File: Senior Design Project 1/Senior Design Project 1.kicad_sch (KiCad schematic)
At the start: 18 parts, among them SW1 SW_Nidec_CAS-120A1, U1 74LS05, U10 74LS08, U11 74LS08, U12 74LS08, U13 74LS08, U2 74HC273, U3 74HC74, U4 74HC74, U5 74HC74, U6 74HC74, U7 74HC74, U8 74HC74, U9 74HC273

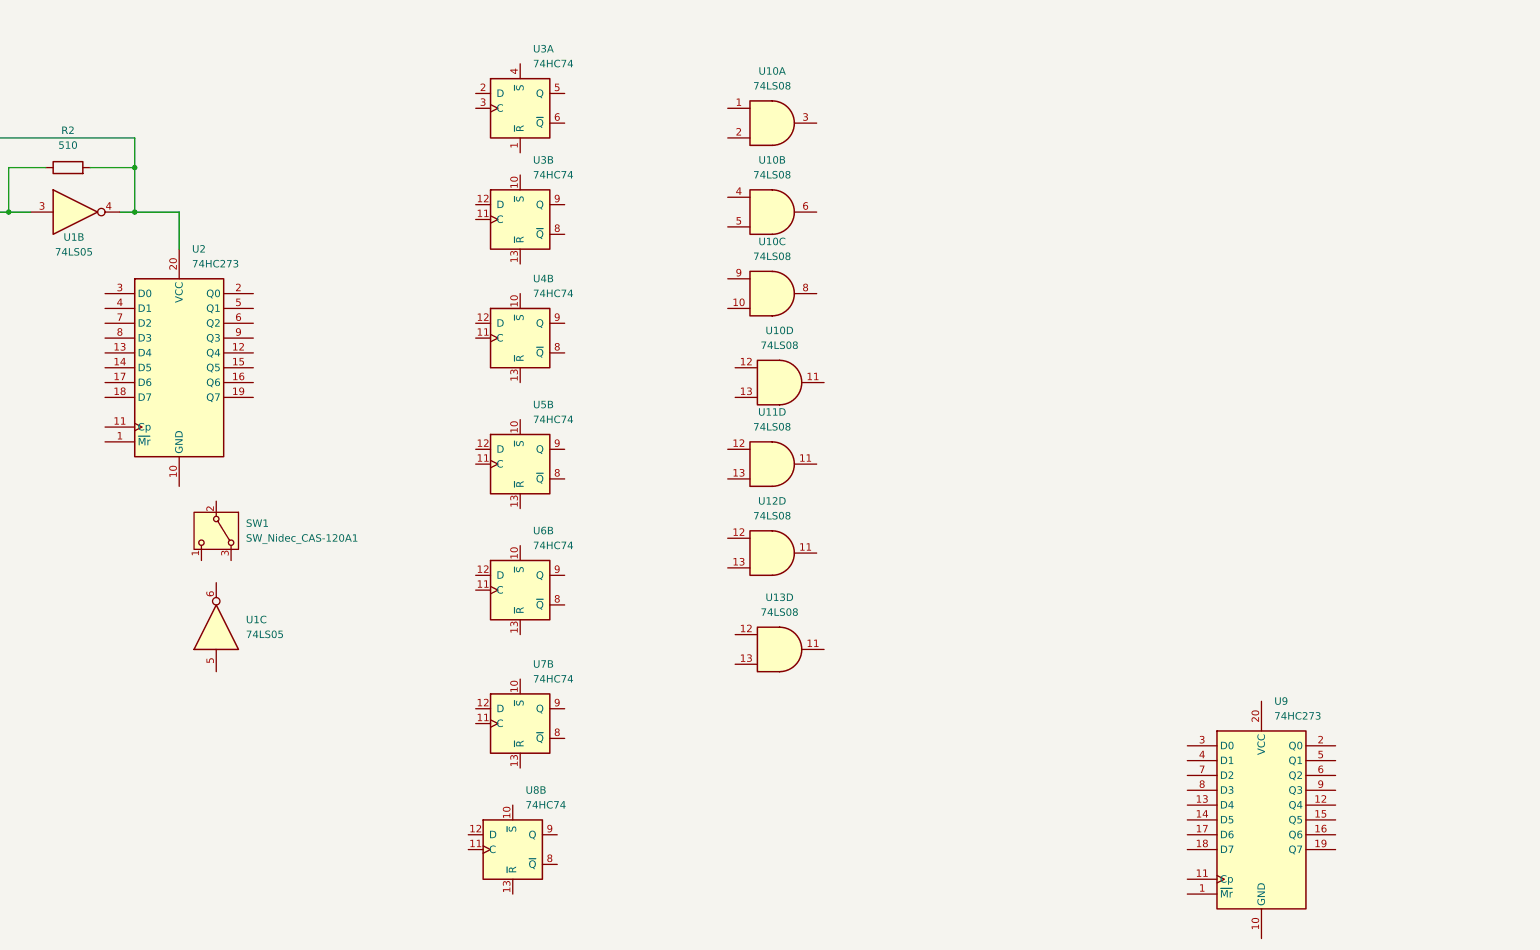
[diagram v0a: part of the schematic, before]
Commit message: Added components & footprints
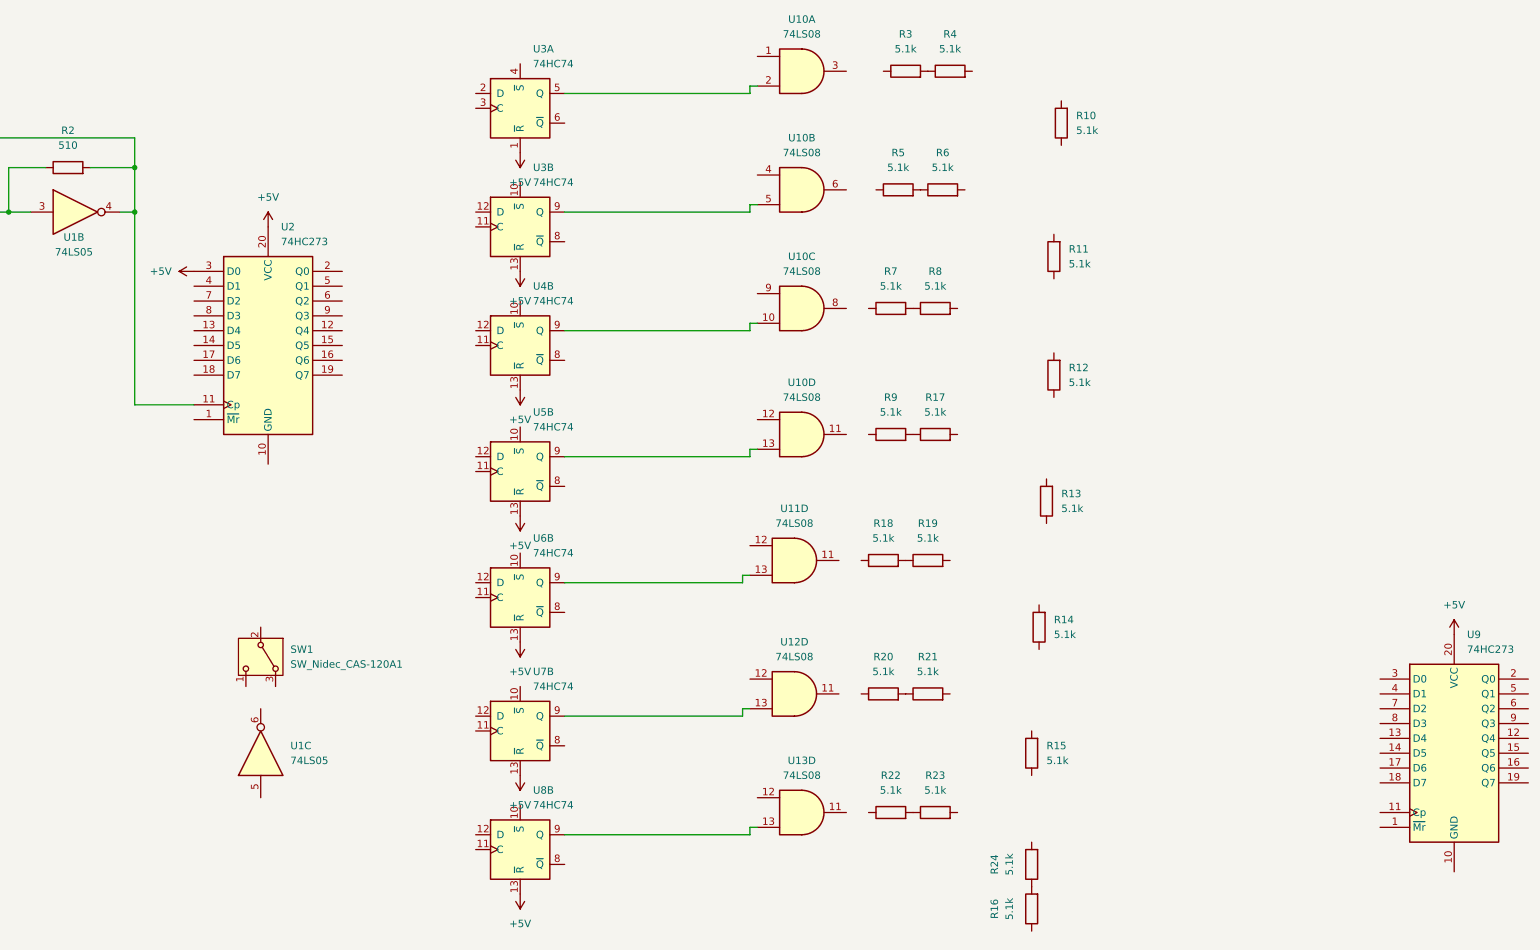
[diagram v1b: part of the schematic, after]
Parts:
- added R10, R11, R12, R13, R14, R15, R16, R17, R18, R19, R20, R21, R22, R23, R24, R3, R4, R5, R6, R7, R8, R9: 5.1k, Resistor_THT:R_Axial_DIN0204_L3.6mm_D1.6mm_P7.62mm_Horizontal, symbol Device:R
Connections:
- net +5V: now reaches U3.13 (~{R})
- net +5V: now also U2.20 (VCC), U2.3 (D0), U3.1 (~{R}), U4.13 (~{R}), U5.13 (~{R}), U6.13 (~{R}), U7.13 (~{R}), U8.13 (~{R}), U9.20 (VCC)
- net at U3.9 (Q): now also U10.5
- net at U10.2: now also U3.5 (Q)
- net at U11.13: now also U6.9 (Q)
- net at C2.2, R2.2, U1.4: now also U2.11 (Cp); no longer U2.20 (VCC)
- net at U13.13: now also U8.9 (Q)
- net at U7.9 (Q): now also U12.13
- net at U4.9 (Q): now also U10.10
- net at U10.13: now also U5.9 (Q)
- new net: R20.2, R21.1
- new net: R22.2, R23.1
- new net: R7.2, R8.1
- new net: R5.2, R6.1
- new net: R16.2, R24.1
- new net: R18.2, R19.1
- new net: R17.1, R9.2
- new net: R3.2, R4.1
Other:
- moved on the sheet: SW1, U10A, U10B, U10C, U10D, U11D, U12D, U13D, U1C, U2, U3B, U4B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

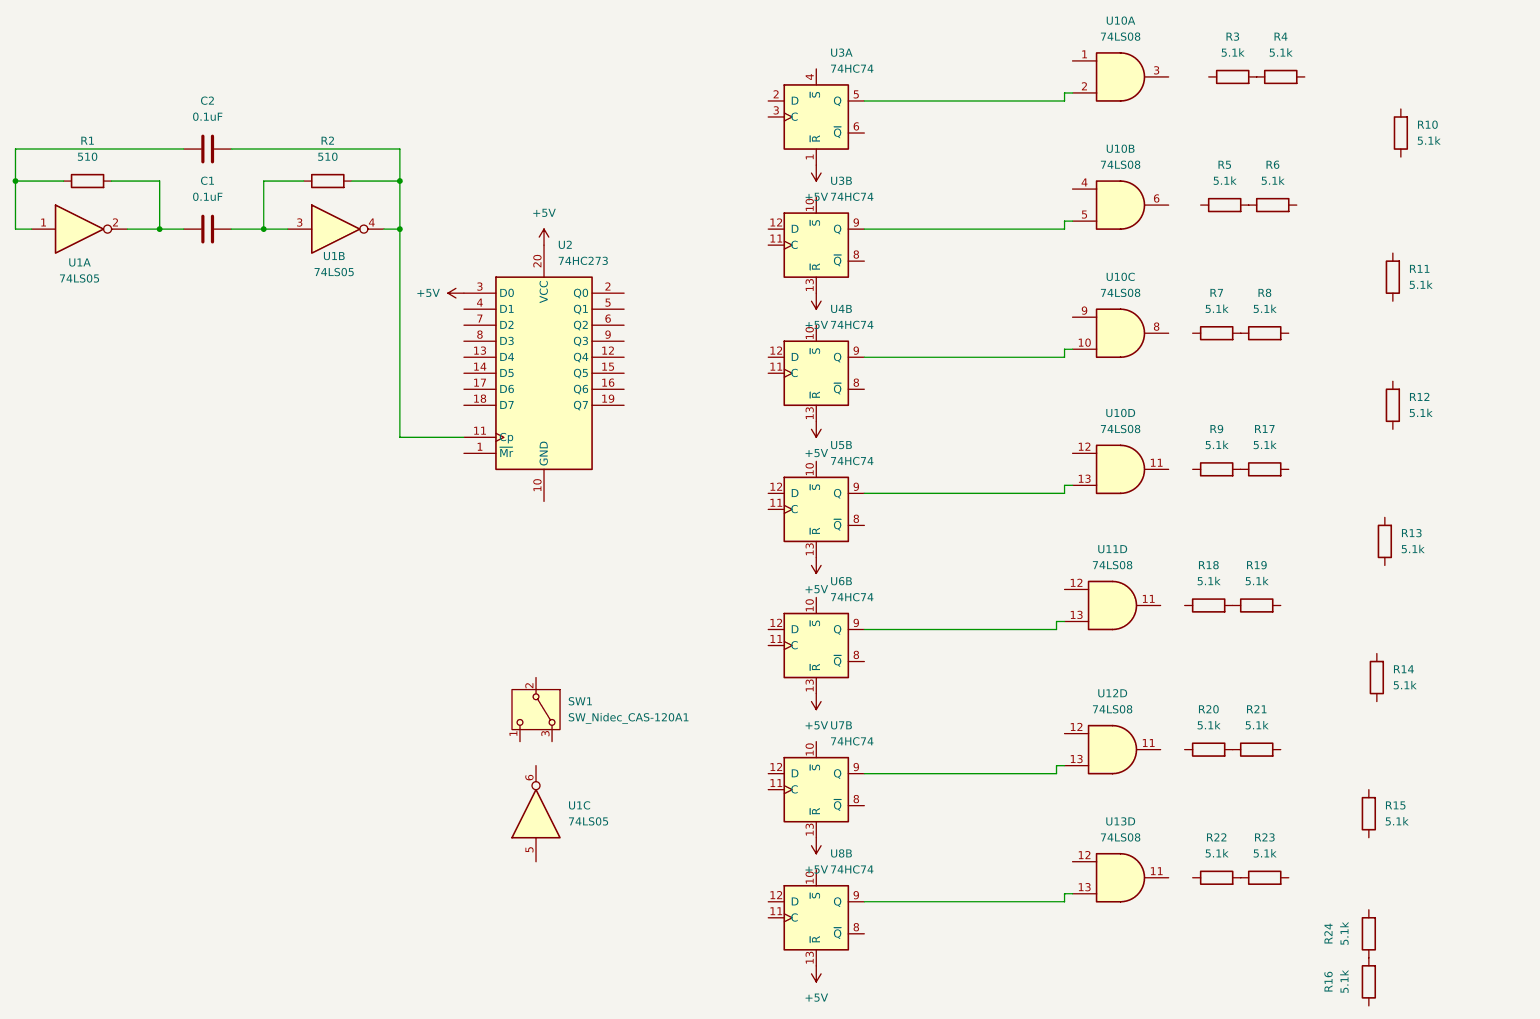
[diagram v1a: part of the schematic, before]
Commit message: Added Flip-Flop Footprint library
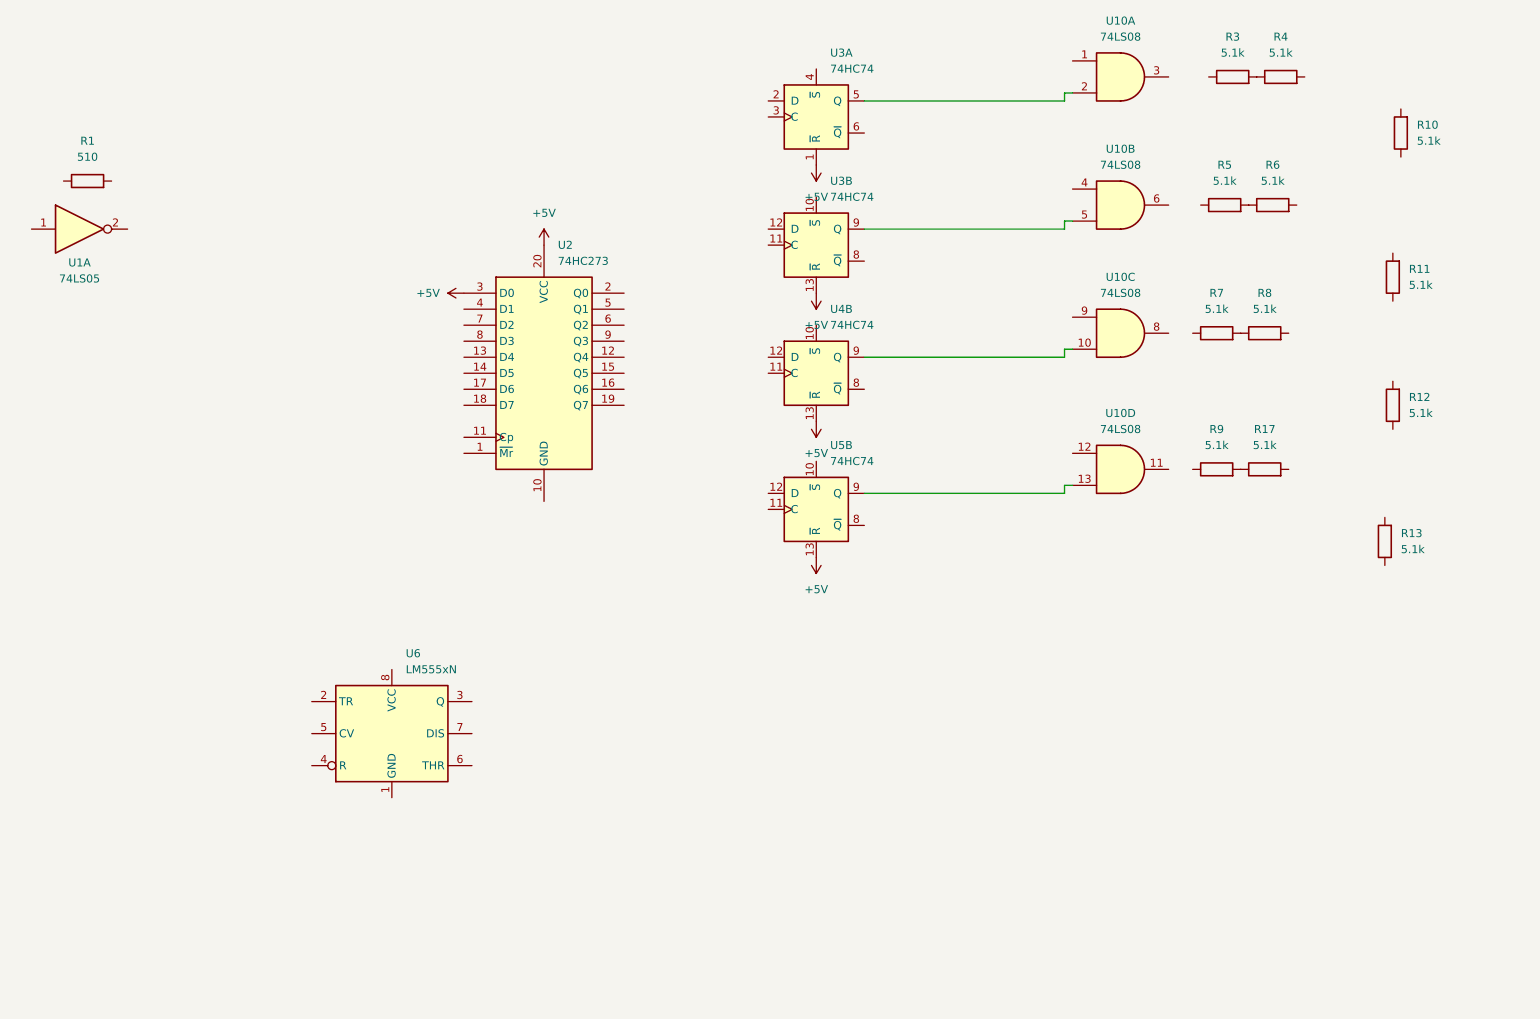
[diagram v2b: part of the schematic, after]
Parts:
- removed C1, C2: 0.1uF, Capacitor_THT:CP_Radial_D4.0mm_P2.00mm, symbol Device:C
- removed R14, R15, R16, R18, R19, R20, R21, R22, R23, R24: 5.1k, Resistor_THT:R_Axial_DIN0204_L3.6mm_D1.6mm_P7.62mm_Horizontal, symbol Device:R
- removed R2: 510, Resistor_THT:R_Axial_DIN0204_L3.6mm_D1.6mm_P7.62mm_Horizontal, symbol Device:R
- removed SW1: SW_Nidec_CAS-120A1, Button_Switch_SMD:Nidec_Copal_CAS-120A, symbol Switch:SW_Nidec_CAS-120A1
- removed unit 2 of U1
- removed unit 3 of U1
- removed U11, U12, U13: 74LS08, symbol 74xx:74LS08
- removed U6, U7, U8: 74HC74, symbol 74xx:74HC74
- added U6: LM555xN, Package_DIP:DIP-8_W7.62mm, symbol Timer:LM555xN
- U10: footprint (none) -> RF_Mini-Circuits:Mini-Circuits_BK377
- U2, U9: footprint (none) -> SN74HC273N:DIP254P762X508-20
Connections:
- net at U1.1: no longer R1.1
- net at U1.2: no longer R1.2

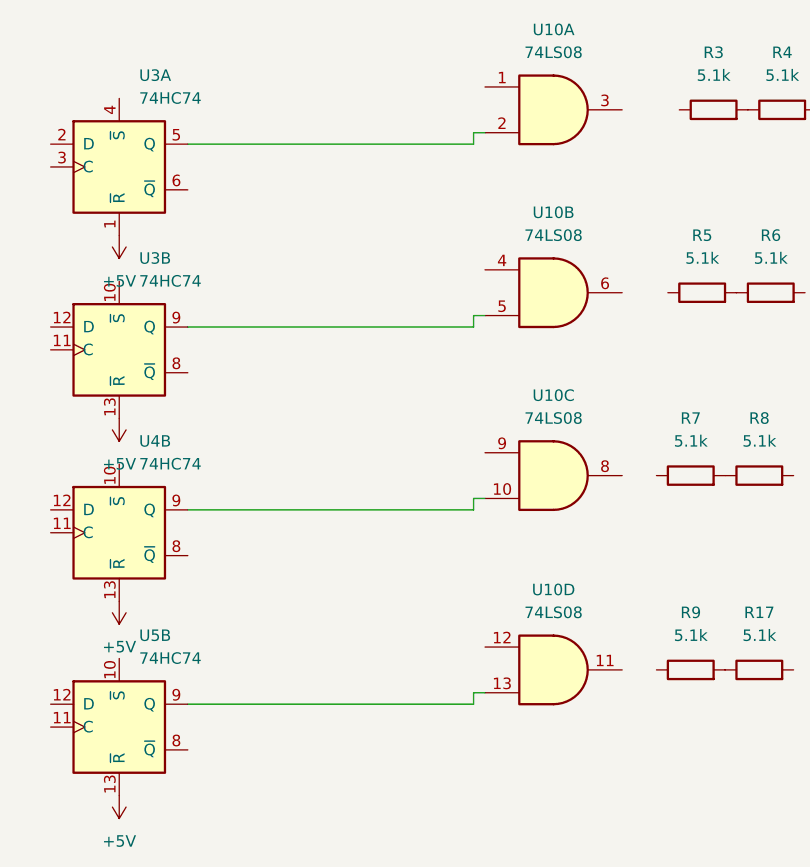
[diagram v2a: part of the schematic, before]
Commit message: Added more libraries
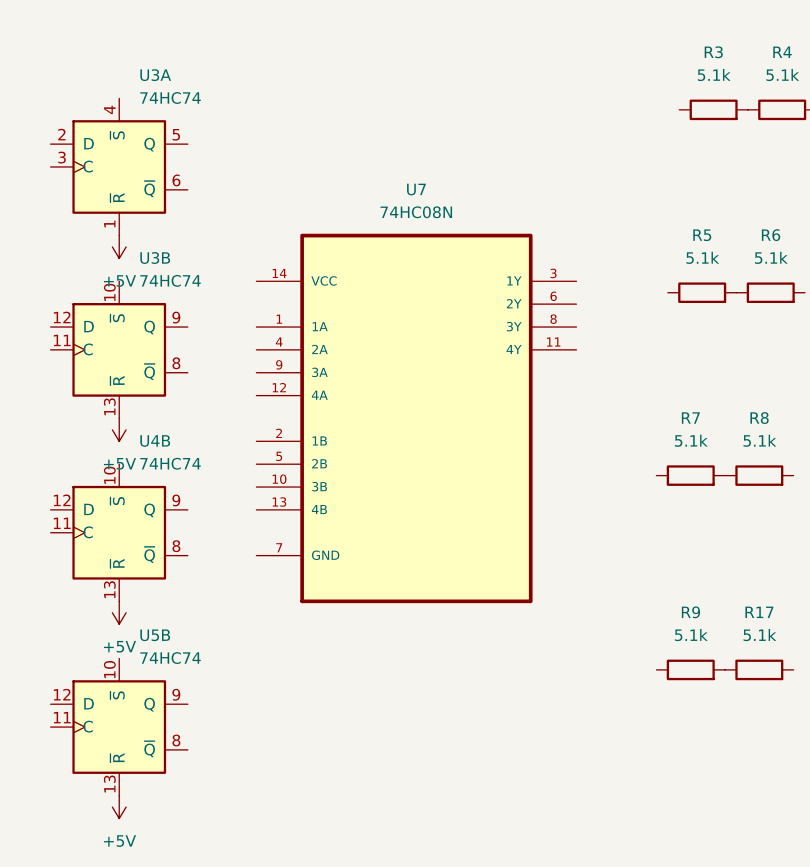
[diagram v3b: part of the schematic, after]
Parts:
- removed U10: 74LS08, RF_Mini-Circuits:Mini-Circuits_BK377, symbol 74xx:74LS08
- added U7: 74HC08N, 74HC08N Library:DIP254P762X420-14, symbol 74HC08N:74HC08N

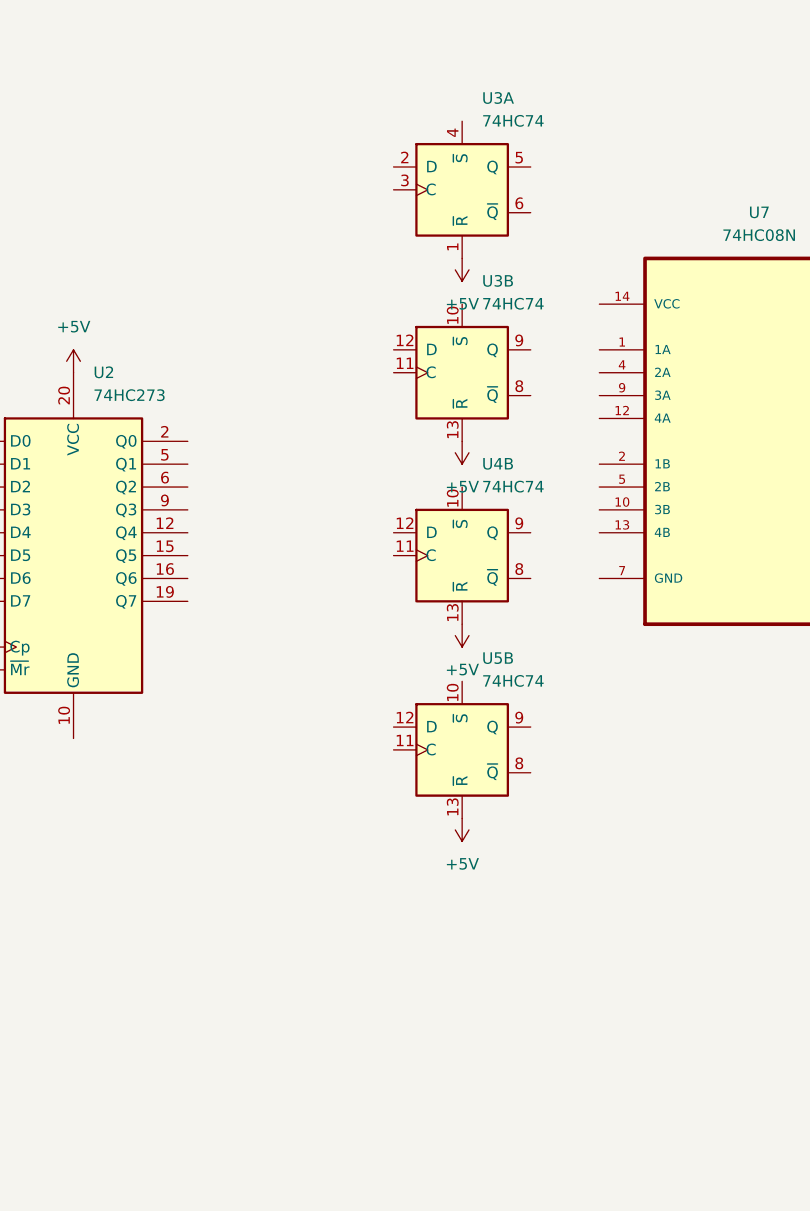
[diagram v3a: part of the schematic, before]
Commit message: Added Dual Flip-flop schematic & footprint
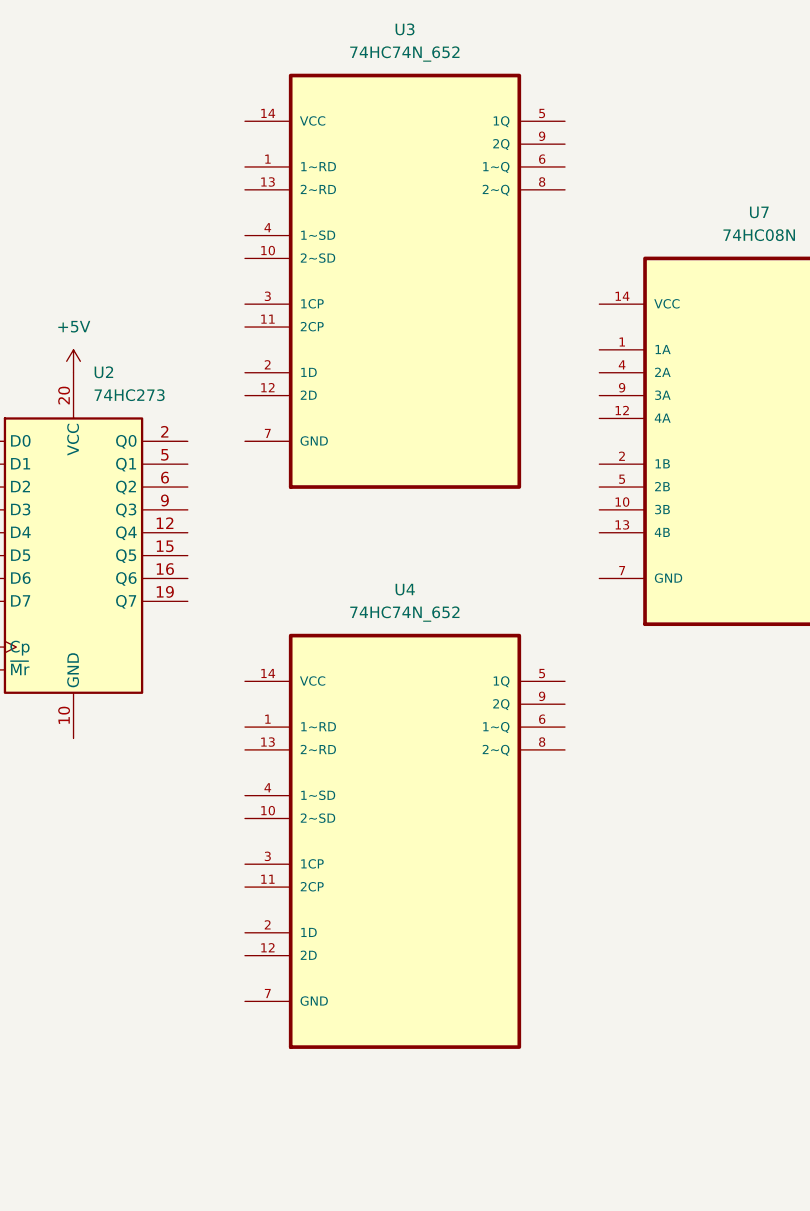
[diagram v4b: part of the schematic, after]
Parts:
- removed U3, U4, U5: 74HC74, symbol 74xx:74HC74
- added U3, U4: 74HC74N_652, 74HC74N_652:DIP254P762X420-14, symbol 74HC74N_652:74HC74N_652
